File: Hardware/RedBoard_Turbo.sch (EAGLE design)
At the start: 61 parts, among them Q1 2.5A/30V, Q2 2N7002PW, U1 MCP73831, U2 74AHC1G125, U3 3.3V, U4 ATSAMD21G-A, U5 W25Q32FV, Y1 32.768kHz

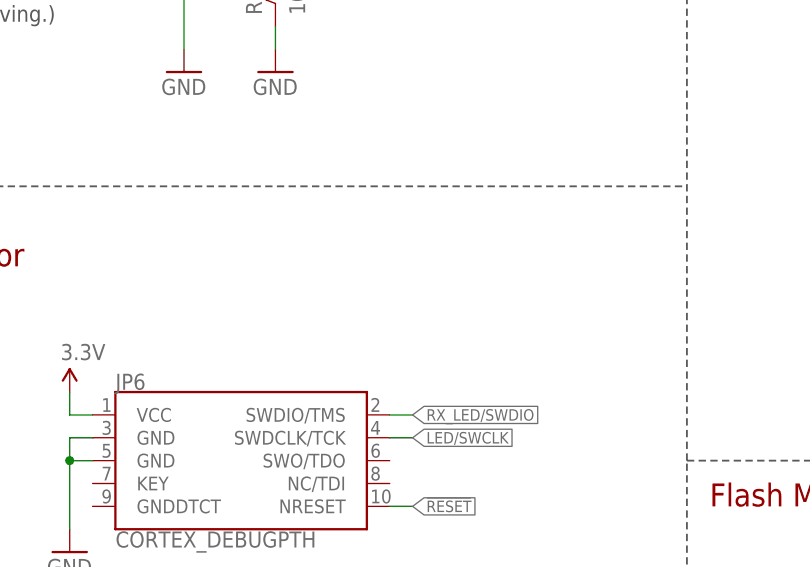
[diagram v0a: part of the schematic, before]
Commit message: Add testpoint and label for LED
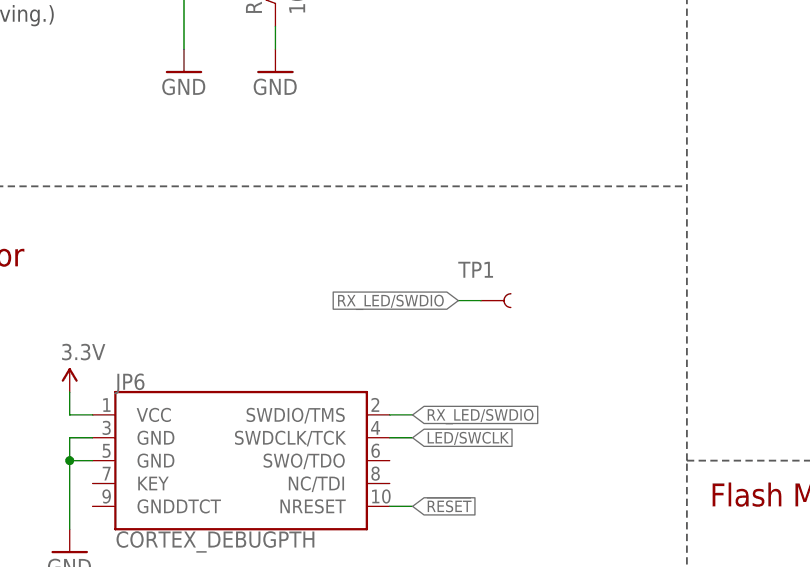
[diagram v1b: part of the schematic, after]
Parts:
- added TP1: TEST-POINTTP_15TH_THRU, SparkFun-Connectors:TEST-POINTTP_15TH_THRU
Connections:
- net RX_LED/SWDIO: now also TP1.1
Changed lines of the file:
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@@
 <part name="FID3" library="SparkFun-Aesthetics" deviceset="FIDUCIAL" device="1X2"/>
 <part name="FID4" library="SparkFun-Aesthetics" deviceset="FIDUCIAL" device="1X2"/>
+<part name="TP1" library="SparkFun-Connectors" deviceset="TEST-POINT" device="TP_15TH_THRU"/>
 </parts>
 <sheets>
@@
 <instance part="FID3" gate="G$1" x="426.72" y="20.32"/>
 <instance part="FID4" gate="G$1" x="426.72" y="17.78"/>
+<instance part="TP1" gate="G$1" x="226.06" y="177.8" smashed="yes">
+<attribute name="NAME" x="223.52" y="180.34" size="1.778" layer="95" font="vector"/>
+</instance>
 </instances>
 <busses>
@@
 <label x="218.44" y="165.1" size="1.27" layer="95" xref="yes"/>
 </segment>
-</net>
+<segment>
+<pinref part="TP1" gate="G$1" pin="1"/>
+<wire x1="226.06" y1="177.8" x2="223.52" y2="177.8" width="0.1524" layer="91"/>
+<label x="223.52" y="177.8" size="1.27" layer="95" rot="R180" xref="yes"/>
+</segment>
+</net>

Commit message: Changes from review
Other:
- note added: "v11"
- note removed: "v10"
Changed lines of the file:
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@@
 <text x="251.46" y="276.86" size="2.54" layer="94" align="top-left">ATSAMD21G</text>
 <text x="337.82" y="10.16" size="2.54" layer="94" align="top-left">Jim Lindblom</text>
-<text x="421.64" y="10.16" size="2.54" layer="94" align="top-left">v10</text>
+<text x="421.64" y="10.16" size="2.54" layer="94" align="top-left">v11</text>
 <wire x1="248.92" y1="0" x2="248.92" y2="35.56" width="0.2032" layer="97" style="longdash"/>
 <text x="43.18" y="40.64" size="1.778" layer="97" rot="R180">Charge Current=

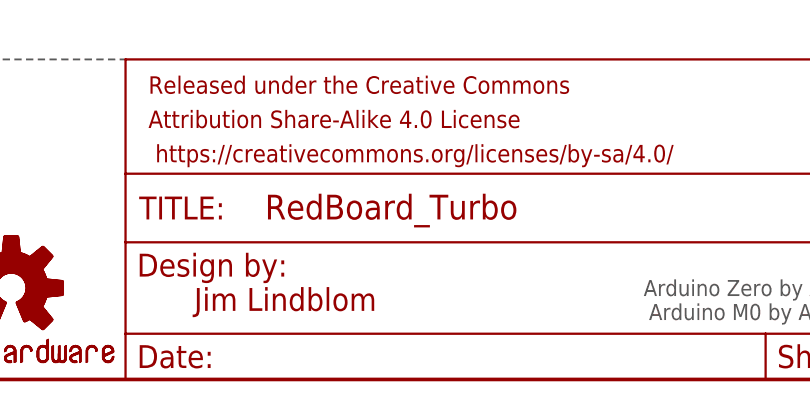
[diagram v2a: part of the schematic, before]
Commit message: Change name on schematic
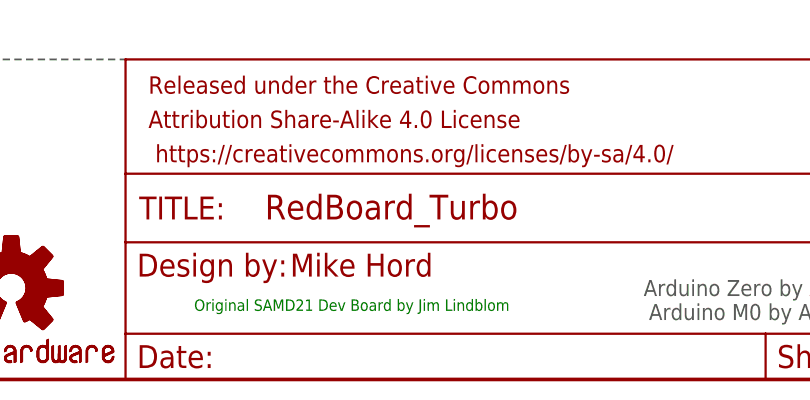
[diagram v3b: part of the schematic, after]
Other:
- note added: "Mike Hord"
- note added: "Original SAMD21 Dev Board by Jim Lindblom"
- note removed: "Jim Lindblom"
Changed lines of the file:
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@@
 <text x="144.78" y="137.16" size="2.54" layer="94" align="top-left">Arduino R3 Headers</text>
 <text x="251.46" y="276.86" size="2.54" layer="94" align="top-left">ATSAMD21G</text>
-<text x="337.82" y="10.16" size="2.54" layer="94" align="top-left">Jim Lindblom</text>
+<text x="348.488" y="13.97" size="2.54" layer="94" align="top-left">Mike Hord</text>
 <text x="421.64" y="10.16" size="2.54" layer="94" align="top-left">v11</text>
 <wire x1="248.92" y1="0" x2="248.92" y2="35.56" width="0.2032" layer="97" style="longdash"/>
@@
 <text x="251.46" y="96.52" size="2.54" layer="94" align="top-left">WS2812 LED</text>
 <text x="251.46" y="157.48" size="2.54" layer="94" align="top-left">Flash Memory</text>
+<text x="337.82" y="7.62" size="1.27" layer="91">Original SAMD21 Dev Board by Jim Lindblom</text>
 </plain>
 <instances>

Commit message: Add polarity markings to JST connector
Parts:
- L1: PROD_ID RES-07859 -> NDUC-07859
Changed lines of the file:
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@@
 <part name="GND23" library="SparkFun-Aesthetics" deviceset="GND" device=""/>
 <part name="L1" library="SparkFun-Passives" deviceset="INDUCTOR" device="0603" value="FB - 30Ohm">
-<attribute name="PROD_ID" value="RES-07859"/>
+<attribute name="PROD_ID" value="NDUC-07859"/>
 </part>
 <part name="GND19" library="SparkFun-Aesthetics" deviceset="GND" device=""/>

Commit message: Updated 0805 cap, approved DRC errors
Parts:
- C3: device SparkFun-Capacitors:1.0UF-25V-+80/-20(0805)" -> SparkFun-Capacitors:1.0UF-0805-25V-10%
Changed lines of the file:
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@@
 <?xml version="1.0" encoding="utf-8"?>
 <!DOCTYPE eagle SYSTEM "eagle.dtd">
-<eagle version="9.0.1">
+<eagle version="8.7.0">
 <drawing>
 <settings>
@@
 <part name="GND17" library="SparkFun-Aesthetics" deviceset="GND" device=""/>
 <part name="D4" library="SparkFun-LED" deviceset="LED-BLUE" device="0603" value="BLUE"/>
-<part name="C3" library="SparkFun-Capacitors" deviceset="1.0UF-25V-+80/-20(0805)" device="&quot;" value="1.0uF"/>
+<part name="C3" library="SparkFun-Capacitors" deviceset="1.0UF" device="-0805-25V-10%" value="1.0uF"/>
 <part name="C5" library="SparkFun-Capacitors" deviceset="2.2UF-10V-20%(0603)" device="" value="2.2uF"/>
 <part name="Q2" library="SparkFun-DiscreteSemi" deviceset="MOSFET-NCHANNEL" device="2N7002PW" value="2N7002PW"/>

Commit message: v20
Updated silk
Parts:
- removed SJ1: R-prog, SparkFun-Passives:JUMPER-PAD-2-NC_BY_TRACE
- LOGO2: value SFE_LOGO_NAME_FLAME.4_INCH -> SFE_LOGO_NAME_FLAME.3_INCH; device SparkFun-Aesthetics:SFE_LOGO_NAME_FLAME.4_INCH -> SparkFun-Aesthetics:SFE_LOGO_NAME_FLAME.3_INCH
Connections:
- removed net N$15: R3.2, SJ1.2, U1.PROG
- net N$13: now also R3.2, U1.PROG; no longer SJ1.1
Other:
- note added: "v20"
- note removed: "v11"

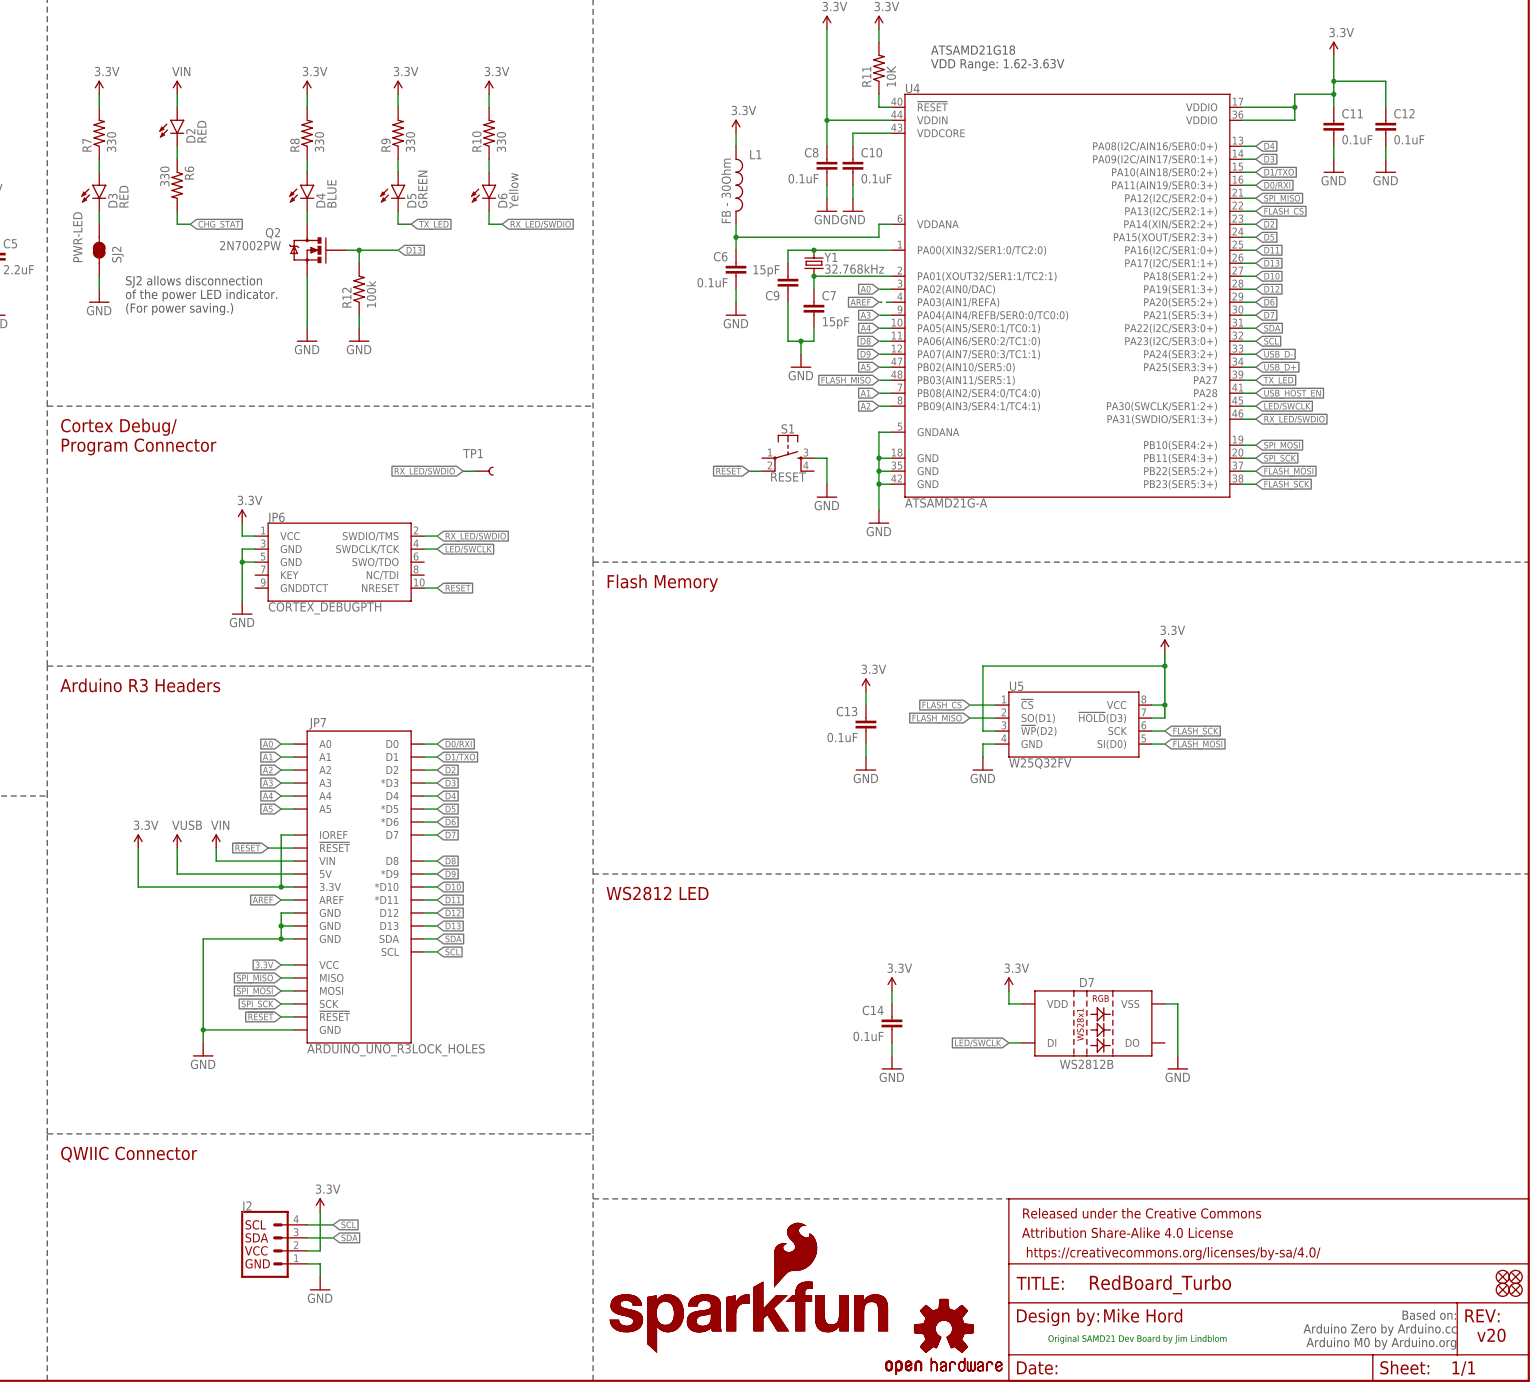
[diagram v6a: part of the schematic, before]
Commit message: Design Review Changes
- Switched board version to v10
- Changed RED charge LED to yellow
- Updated power LED silk
- Added barrel jack max voltage silk
- Replaced reset button with larger button and longer actuator
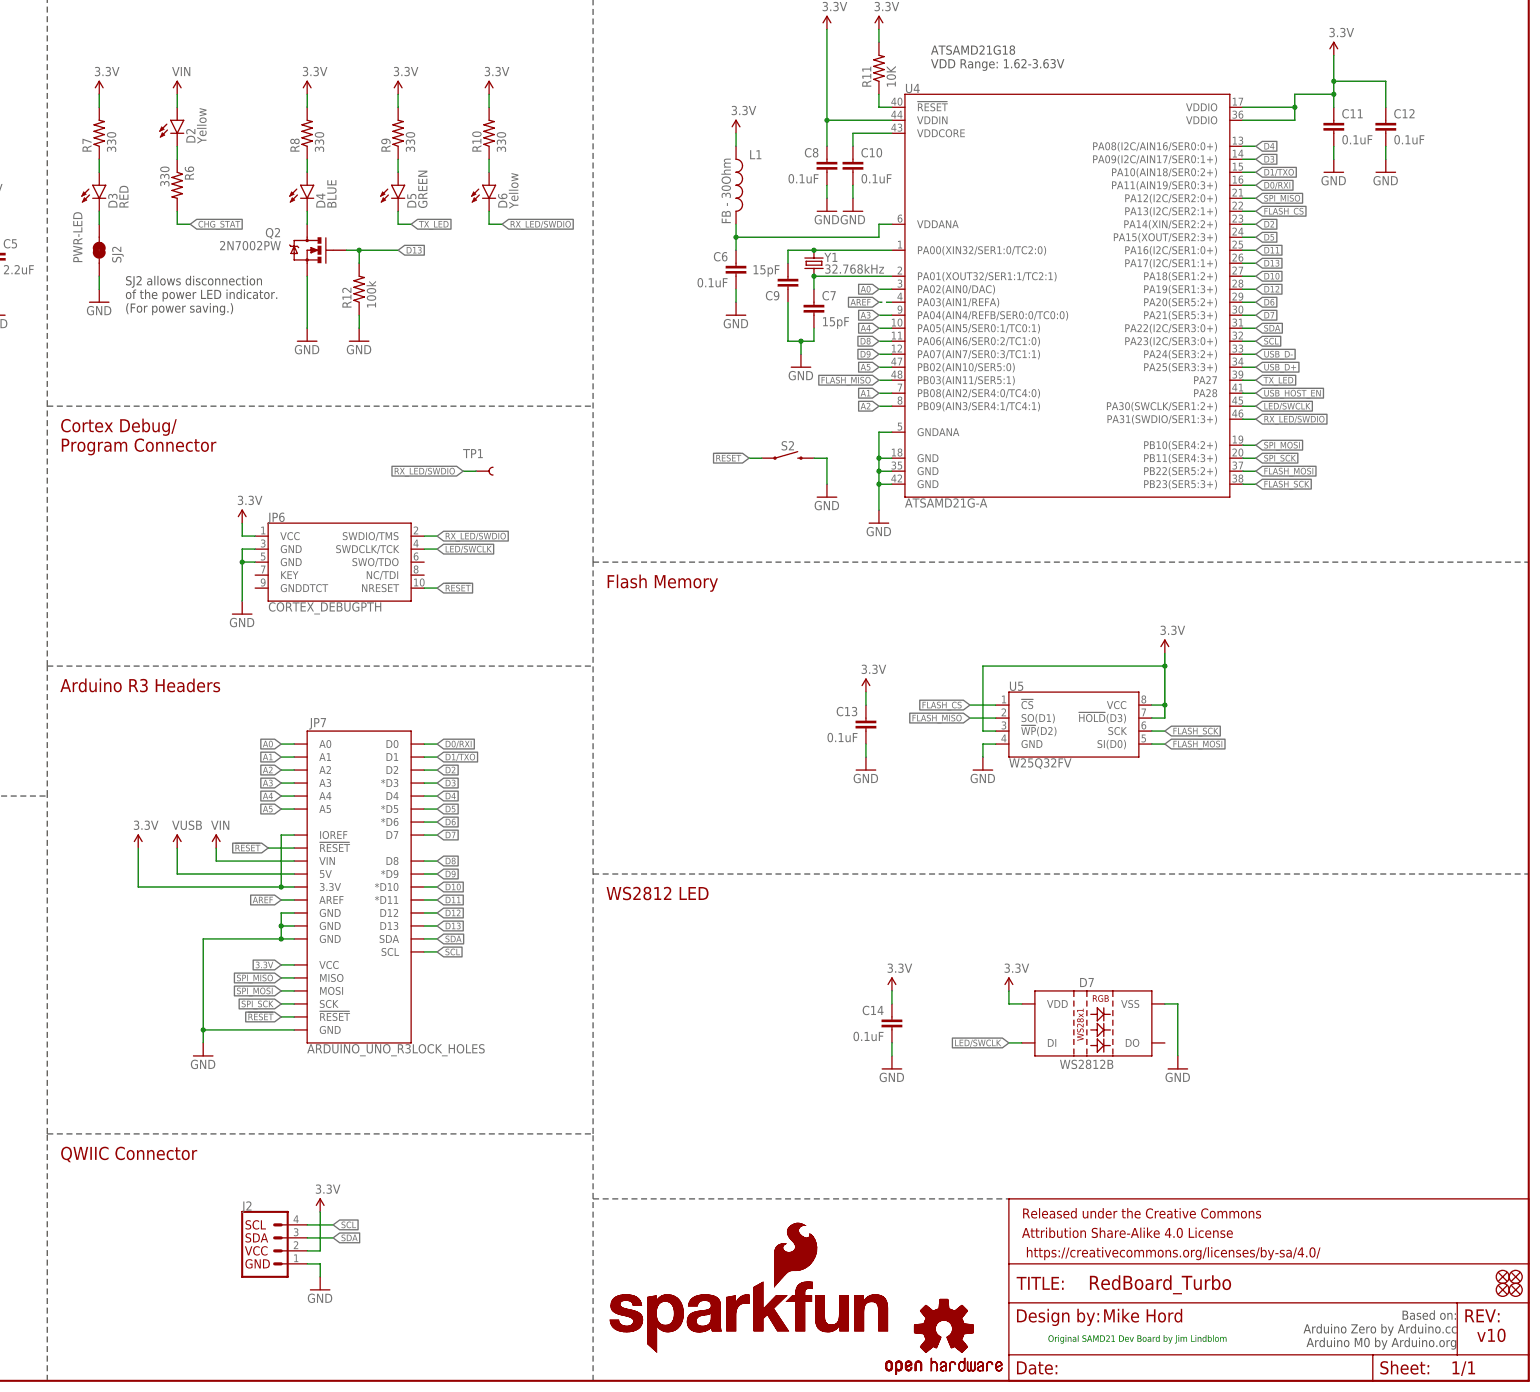
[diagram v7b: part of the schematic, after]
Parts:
- removed S1: RESET, SparkFun-Switches:MOMENTARY-SWITCH-SPST-2-SMD-4.6X2.8MM
- added S2: MOMENTARY-SWITCH-SPST-SMD-5.2-TALL-REDUNDANT, SparkFun-Switches:MOMENTARY-SWITCH-SPST-SMD-5.2-TALL-REDUNDANT
- D2: value RED -> Yellow; device SparkFun-LED:LED-RED0603 -> SparkFun-LED:LED-YELLOW0603
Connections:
- net !RESET: now also S2.1; no longer S1.2
- net GND: now also S2.2; no longer S1.3
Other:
- note added: "v10"
- note removed: "v20"
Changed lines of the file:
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@@
 <part name="LOGO1" library="SparkFun-Aesthetics" deviceset="SFE_LOGO_NAME_FLAME" device=".2_INCH" value="SFE_LOGO_NAME_FLAME.2_INCH"/>
 <part name="SJ2" library="SparkFun-Passives" deviceset="JUMPER-PAD-2-NC_BY_TRACE" device="NO_SILK" value="PWR-LED"/>
-<part name="S1" library="SparkFun-Switches" deviceset="MOMENTARY-SWITCH-SPST-2" device="-SMD-4.6X2.8MM" value="RESET"/>
 <part name="FID2" library="SparkFun-Aesthetics" deviceset="FIDUCIAL" device="1X2"/>
 <part name="FID1" library="SparkFun-Aesthetics" deviceset="FIDUCIAL" device="1X2"/>
@@
 <part name="R1" library="SparkFun-Resistors" deviceset="3.9KOHM1/10W1%(0603)" device="" value="3.9K"/>
 <part name="GND4" library="SparkFun-Aesthetics" deviceset="GND" device=""/>
-<part name="D2" library="SparkFun-LED" deviceset="LED-RED" device="0603" value="RED"/>
+<part name="D2" library="SparkFun-LED" deviceset="LED-YELLOW" device="0603" value="Yellow"/>
 <part name="R6" library="SparkFun-Resistors" deviceset="330OHM1/10W1%(0603)" device="" value="330"/>
 <part name="R3" library="SparkFun-Passives" deviceset="RESISTOR" device="PTH-1/6W" value="PROG"/>
@@
 <part name="FID4" library="SparkFun-Aesthetics" deviceset="FIDUCIAL" device="1X2"/>
 <part name="TP1" library="SparkFun-Connectors" deviceset="TEST-POINT" device="TP_15TH_THRU"/>
+<part name="S2" library="SparkFun-Switches" deviceset="MOMENTARY-SWITCH-SPST" device="-SMD-5.2-TALL-REDUNDANT" value=""/>
 </parts>
 <sheets>
@@
 <text x="251.46" y="276.86" size="2.54" layer="94" align="top-left">ATSAMD21G</text>
 <text x="348.488" y="13.97" size="2.54" layer="94" align="top-left">Mike Hord</text>
-<text x="421.64" y="10.16" size="2.54" layer="94" align="top-left">v20</text>
+<text x="421.64" y="10.16" size="2.54" layer="94" align="top-left">v10</text>
 <wire x1="248.92" y1="0" x2="248.92" y2="35.56" width="0.2032" layer="97" style="longdash"/>
 <text x="43.18" y="40.64" size="1.778" layer="97" rot="R180">Charge Current=
@@
 <attribute name="VALUE" x="147.32" y="218.44" size="1.778" layer="96" rot="MR90"/>
 </instance>
-<instance part="S1" gate="G$1" x="287.02" y="180.34" smashed="yes">
-<attribute name="NAME" x="287.02" y="185.166" size="1.778" layer="95" font="vector" align="bottom-center"/>
-<attribute name="VALUE" x="287.02" y="177.546" size="1.778" layer="96" font="vector" align="top-center"/>
-</instance>
 <instance part="FID2" gate="G$1" x="429.26" y="17.78" smashed="yes"/>
 <instance part="FID1" gate="G$1" x="429.26" y="20.32" smashed="yes"/>
@@
 <attribute name="NAME" x="223.52" y="180.34" size="1.778" layer="95" font="vector"/>
 </instance>
+<instance part="S2" gate="G$1" x="287.02" y="180.34"/>
 </instances>
 <busses>
@@
 <pinref part="GND22" gate="1" pin="GND"/>
 <wire x1="294.64" y1="175.26" x2="294.64" y2="180.34" width="0.1524" layer="91"/>
-<pinref part="S1" gate="G$1" pin="3"/>
 <wire x1="294.64" y1="180.34" x2="292.1" y2="180.34" width="0.1524" layer="91"/>
+<pinref part="S2" gate="G$1" pin="2"/>
 </segment>
 <segment>
@@
 </segment>
 <segment>
-<pinref part="S1" gate="G$1" pin="2"/>
-<wire x1="281.94" y1="177.8" x2="279.4" y2="177.8" width="0.1524" layer="91"/>
-<label x="279.4" y="177.8" size="1.27" layer="95" rot="R180" xref="yes"/>
+<wire x1="281.94" y1="180.34" x2="279.4" y2="180.34" width="0.1524" layer="91"/>
+<label x="279.4" y="180.34" size="1.27" layer="95" rot="R180" xref="yes"/>
+<pinref part="S2" gate="G$1" pin="1"/>
 </segment>
 </net>
